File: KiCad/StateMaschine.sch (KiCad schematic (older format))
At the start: 28 parts, among them U27 74LVC1G04, U28 74HC164, U29 74LVC1G175, U30 74HC02, U31 74HC02

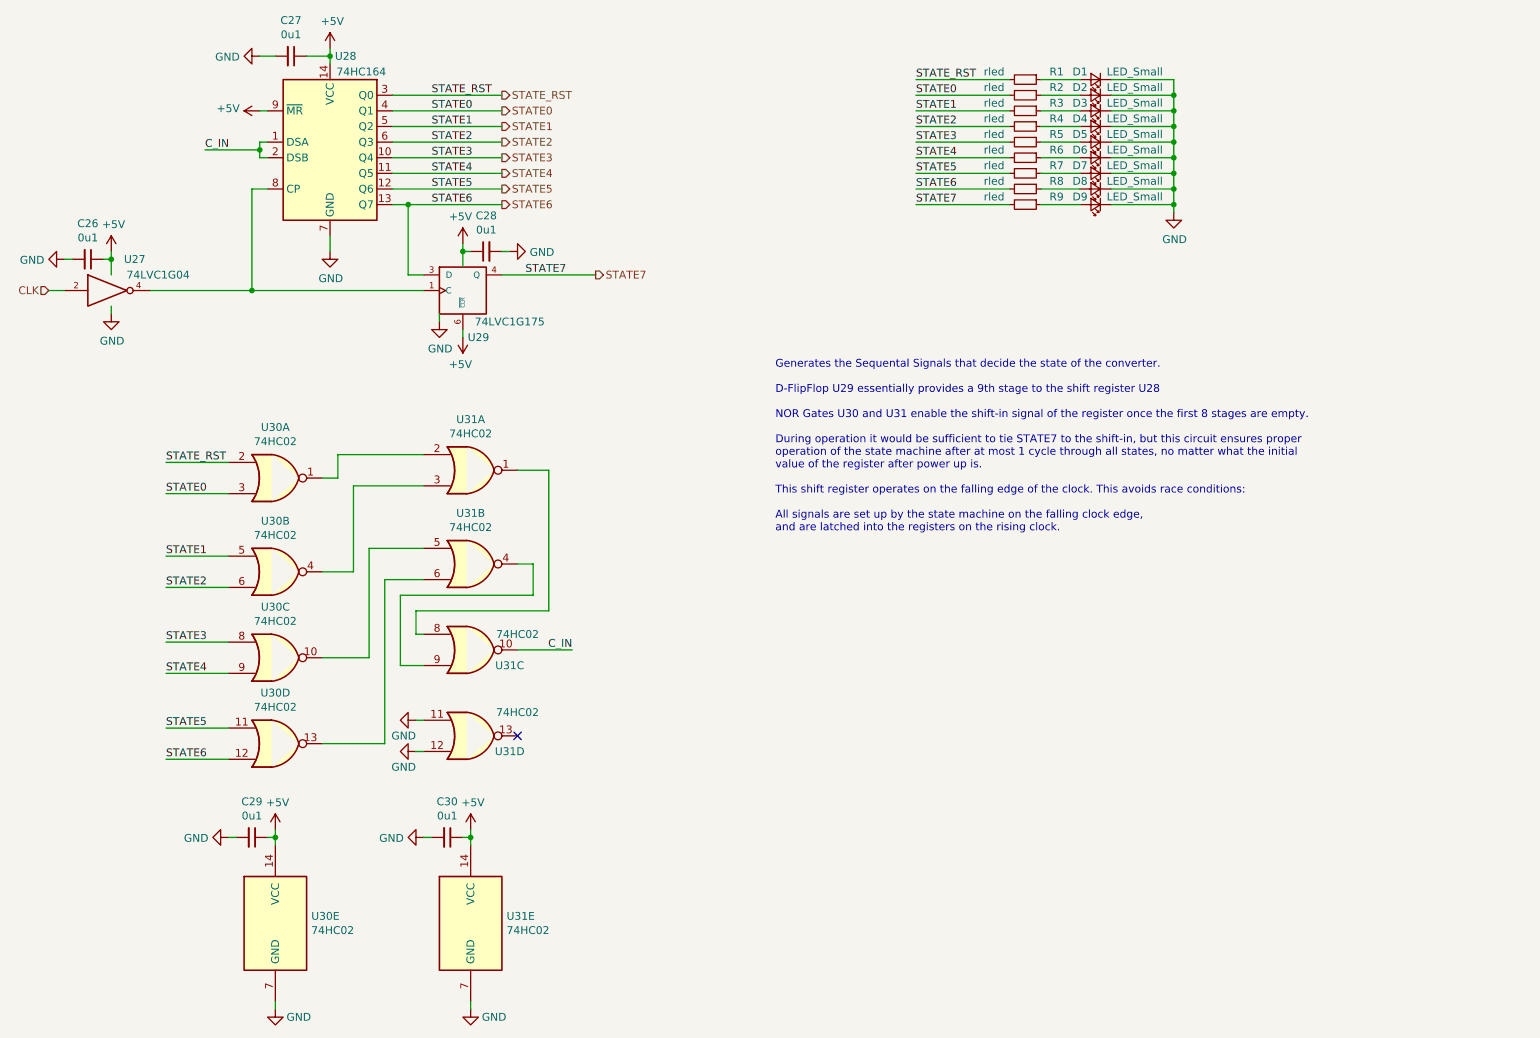
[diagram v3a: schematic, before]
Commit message: Fixed State Numbering/Wiring Order
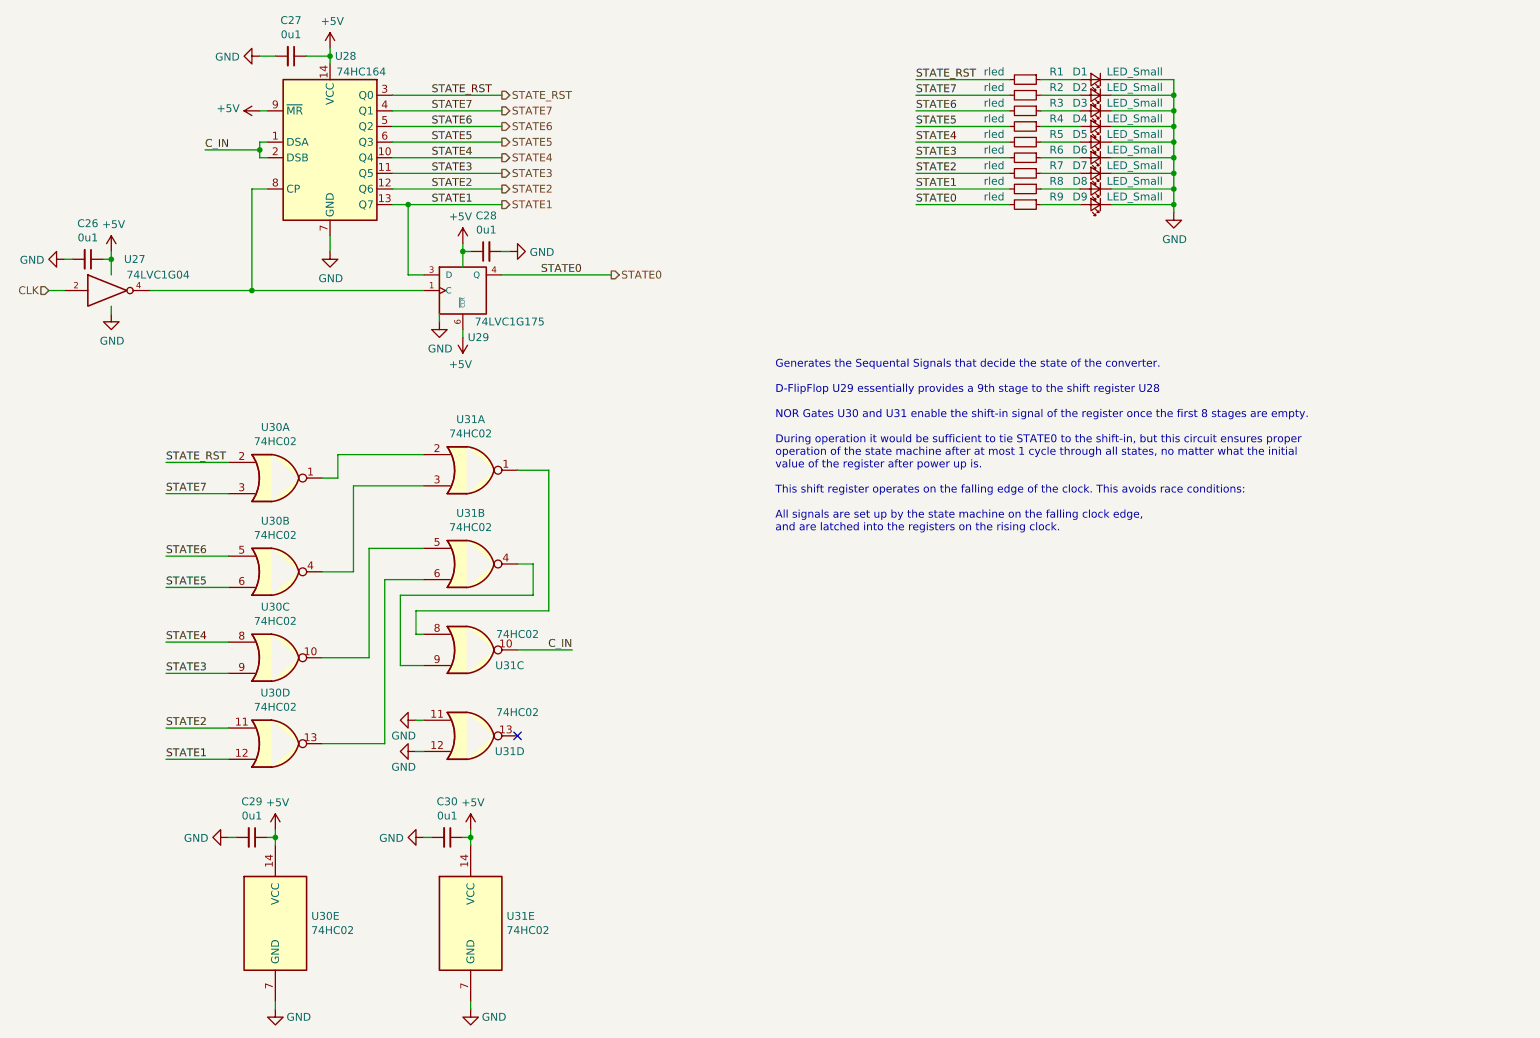
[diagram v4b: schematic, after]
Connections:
- net STATE0: now also R9.2, U29.4 (Q); no longer R2.2, U28.4 (Q1), U30.3
- net STATE1: now also R8.2, U28.13 (Q7), U29.3 (D), U30.12; no longer R3.2, U28.5 (Q2), U30.5
- net STATE2: now also R7.2, U28.12 (Q6), U30.11; no longer R4.2, U28.6 (Q3), U30.6
- net STATE3: now also R6.2, U28.11 (Q5), U30.9; no longer R5.2, U28.10 (Q4), U30.8
- net STATE4: now also R5.2, U28.10 (Q4), U30.8; no longer R6.2, U28.11 (Q5), U30.9
- net STATE5: now also R4.2, U28.6 (Q3), U30.6; no longer R7.2, U28.12 (Q6), U30.11
- net STATE6: now also R3.2, U28.5 (Q2), U30.5; no longer R8.2, U28.13 (Q7), U29.3 (D), U30.12
- net STATE7: now also R2.2, U28.4 (Q1), U30.3; no longer R9.2, U29.4 (Q)
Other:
- note added: "Generates the Sequental Signals that decide the state of the converter.\n\nD-FlipFlop U29 essentially provides a 9th stage to the shift register U28\n\nNOR Gates U30 and U31 enable the shift-in signal of the register once the first 8 stages are empty. \n\nDuring operation it would be sufficient to tie STATE0 to the shift-in, but this circuit ensures proper \noperation of the state machine after a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"
- note removed: "Generates the Sequental Signals that decide the state of the converter.\n\nD-FlipFlop U29 essentially provides a 9th stage to the shift register U28\n\nNOR Gates U30 and U31 enable the shift-in signal of the register once the first 8 stages are empty. \n\nDuring operation it would be sufficient to tie STATE7 to the shift-in, but this circuit ensures proper \noperation of the state machine after a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"
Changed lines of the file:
@@
 $Descr A4 11693 8268
 encoding utf-8
-Sheet 8 9
+Sheet 7 9
 Title "Schilk_SA-ADC"
 Date "2020-02-03"
@@
 Text HLabel 1950 2950 0    50   Input ~ 0
 CLK
+Text Label 7500 2400 0    50   ~ 0
+STATE0
+Text Label 7500 2300 0    50   ~ 0
+STATE1
+Text Label 7500 2200 0    50   ~ 0
+STATE2
+Text Label 7500 2100 0    50   ~ 0
+STATE3
+Text Label 7500 2000 0    50   ~ 0
+STATE4
+Text Label 7500 1900 0    50   ~ 0
+STATE5
+Text Label 7500 1800 0    50   ~ 0
+STATE6
 Text Label 7500 1700 0    50   ~ 0
-STATE0
-Text Label 7500 1800 0    50   ~ 0
-STATE1
-Text Label 7500 1900 0    50   ~ 0
-STATE2
-Text Label 7500 2000 0    50   ~ 0
-STATE3
-Text Label 7500 2100 0    50   ~ 0
-STATE4
-Text Label 7500 2200 0    50   ~ 0
-STATE5
-Text Label 7500 2300 0    50   ~ 0
-STATE6
-Text Label 7500 2400 0    50   ~ 0
 STATE7
 $Comp
@@
 	8750 2400 9150 2400
 Wire Wire Line
+	7500 2400 8100 2400
+Wire Wire Line
+	7500 2300 8100 2300
+Wire Wire Line
+	7500 2200 8100 2200
+Wire Wire Line
+	7500 2100 8100 2100
+Wire Wire Line
+	7500 2000 8100 2000
+Wire Wire Line
+	7500 1900 8100 1900
+Wire Wire Line
+	7500 1800 8100 1800
+Wire Wire Line
 	7500 1700 8100 1700
-Wire Wire Line
-	7500 1800 8100 1800
-Wire Wire Line
-	7500 1900 8100 1900
-Wire Wire Line
-	7500 2000 8100 2000
-Wire Wire Line
-	7500 2100 8100 2100
-Wire Wire Line
-	7500 2200 8100 2200
-Wire Wire Line
-	7500 2300 8100 2300
-Wire Wire Line
-	7500 2400 8100 2400
 Wire Wire Line
 	9150 1600 9150 1700
@@
 Wire Wire Line
 	9150 2400 9150 2450
+Text Label 4400 2400 0    50   ~ 0
+STATE1
+Text Label 4400 2300 0    50   ~ 0
+STATE2
+Text Label 4400 2200 0    50   ~ 0
+STATE3
+Text Label 4400 2100 0    50   ~ 0
+STATE4
+Text Label 4400 2000 0    50   ~ 0
+STATE5
+Text Label 4400 1900 0    50   ~ 0
+STATE6
 Text Label 4400 1800 0    50   ~ 0
-STATE0
-Text Label 4400 1900 0    50   ~ 0
-STATE1
-Text Label 4400 2000 0    50   ~ 0
-STATE2
-Text Label 4400 2100 0    50   ~ 0
-STATE3
-Text Label 4400 2200 0    50   ~ 0
-STATE4
-Text Label 4400 2300 0    50   ~ 0
-STATE5
-Text Label 4400 2400 0    50   ~ 0
-STATE6
-Text Label 5000 2850 0    50   ~ 0
 STATE7
 Text Label 4400 1700 0    50   ~ 0
 STATE_RST
-Wire Wire Line
-	4250 2400 4850 2400
-Wire Wire Line
-	4850 2850 5450 2850
-Text HLabel 4850 1800 2    50   Output ~ 0
-STATE0
-Text HLabel 4850 1900 2    50   Output ~ 0
-STATE1
-Text HLabel 4850 2000 2    50   Output ~ 0
-STATE2
-Text HLabel 4850 2100 2    50   Output ~ 0
-STATE3
-Text HLabel 4850 2200 2    50   Output ~ 0
-STATE4
-Text HLabel 4850 2300 2    50   Output ~ 0
-STATE5
-Text HLabel 4850 2400 2    50   Output ~ 0
-STATE6
-Text HLabel 5450 2850 2    50   Output ~ 0
-STATE7
 Text HLabel 4850 1700 2    50   Output ~ 0
 STATE_RST
-Connection ~ 4250 2400
 Wire Wire Line
 	4150 1700 4850 1700
 Wire Wire Line
-	4150 1800 4850 1800
-Wire Wire Line
-	4150 1900 4850 1900
+	4150 2300 4850 2300
+Wire Wire Line
+	4150 2200 4850 2200
+Wire Wire Line
+	4150 2100 4850 2100
 Wire Wire Line
 	4150 2000 4850 2000
-Wire Wire Line
-	4150 2100 4850 2100
-Wire Wire Line
-	4150 2200 4850 2200
-Wire Wire Line
-	4150 2300 4850 2300
 Text Label 7500 1600 0    50   ~ 0
 STATE_RST
@@
 Wire Wire Line
 	3400 7550 3400 7500
-Text Label 2700 4650 0    50   ~ 0
-STATE1
-Text Label 2700 4850 0    50   ~ 0
-STATE2
-Text Label 2700 5200 0    50   ~ 0
-STATE3
-Text Label 2700 5400 0    50   ~ 0
-STATE4
-Text Label 2700 5750 0    50   ~ 0
-STATE5
-Text Label 2700 5950 0    50   ~ 0
-STATE6
 Text Label 2700 4050 0    50   ~ 0
 STATE_RST
-Text Label 2700 4250 0    50   ~ 0
-STATE0
 Wire Wire Line
 	2700 4050 3100 4050
-Wire Wire Line
-	2700 4250 3100 4250
-Wire Wire Line
-	2700 4650 3100 4650
-Wire Wire Line
-	2700 4850 3100 4850
-Wire Wire Line
-	2700 5200 3100 5200
-Wire Wire Line
-	2700 5400 3100 5400
-Wire Wire Line
-	2700 5750 3100 5750
-Wire Wire Line
-	2700 5950 3100 5950
 $Comp
 L 74xx:74HC02 U31
@@
 	3300 2050 3300 2100
 Text Notes 6600 4500 0    50   ~ 0
-Generates the Sequental Signals that decide the state of the converter.\n\nD-FlipFlop U29 essentially provides a 9th stage to the shift register U28\n\nNOR Gates U30 and U31 enable the shift-in signal of the register once the first 8 stages are empty. \n\nDuring operation it would be sufficient to tie STATE7 to the shift-in, but this circuit ensures proper \noperation of the state machine after at most 1 cycle through all states, no matter what the initial\nvalue of the register after power up is.\n\nThis shift register operates on the falling edge of the clock. This avoids race conditions:\n\nAll signals are set up by the state machine on the falling clock edge,\nand are latched into the registers on the rising clock.
+Generates the Sequental Signals that decide the state of the converter.\n\nD-FlipFlop U29 essentially provides a 9th stage to the shift register U28\n\nNOR Gates U30 and U31 enable the shift-in signal of the register once the first 8 stages are empty. \n\nDuring operation it would be sufficient to tie STATE0 to the shift-in, but this circuit ensures proper \noperation of the state machine after at most 1 cycle through all states, no matter what the initial\nvalue of the register after power up is.\n\nThis shift register operates on the falling edge of the clock. This avoids race conditions:\n\nAll signals are set up by the state machine on the falling clock edge,\nand are latched into the registers on the rising clock.
+Text HLabel 4850 1900 2    50   Output ~ 0
+STATE6
+Text HLabel 4850 2000 2    50   Output ~ 0
+STATE5
+Text HLabel 4850 2100 2    50   Output ~ 0
+STATE4
+Text HLabel 4850 2200 2    50   Output ~ 0
+STATE3
+Text HLabel 4850 2300 2    50   Output ~ 0
+STATE2
+Text HLabel 4850 2400 2    50   Output ~ 0
+STATE1
+Text HLabel 5550 2850 2    50   Output ~ 0
+STATE0
+Text HLabel 4850 1800 2    50   Output ~ 0
+STATE7
+Wire Wire Line
+	4150 1800 4850 1800
+Wire Wire Line
+	4150 1900 4850 1900
+Wire Wire Line
+	4850 2850 5550 2850
+Text Label 5100 2850 0    50   ~ 0
+STATE0
+Connection ~ 4250 2400
+Wire Wire Line
+	4250 2400 4850 2400
+Text Label 2700 5950 0    50   ~ 0
+STATE1
+Text Label 2700 5750 0    50   ~ 0
+STATE2
+Text Label 2700 5400 0    50   ~ 0
+STATE3
+Text Label 2700 5200 0    50   ~ 0
+STATE4
+Text Label 2700 4850 0    50   ~ 0
+STATE5
+Text Label 2700 4650 0    50   ~ 0
+STATE6
+Text Label 2700 4250 0    50   ~ 0
+STATE7
+Wire Wire Line
+	2700 5950 3100 5950
+Wire Wire Line
+	2700 5750 3100 5750
+Wire Wire Line
+	2700 5400 3100 5400
+Wire Wire Line
+	2700 5200 3100 5200
+Wire Wire Line
+	2700 4850 3100 4850
+Wire Wire Line
+	2700 4650 3100 4650
+Wire Wire Line
+	2700 4250 3100 4250
 $EndSCHEMATC
